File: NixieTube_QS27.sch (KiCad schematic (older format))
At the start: 56 parts, among them J1 Conn_01x06_Male, J2 HV_IN, J3 Conn_01x06_Female, J4 HV_OUT, Q1 MMBTA42LT1, Q10 MMBTA42LT1, Q11 AO3400, Q12 AO3400, Q13 AO3400, Q14 MMBTA42LT1, Q15 MMBTA42LT1, Q2 MMBTA42LT1, Q3 MMBTA42LT1, Q4 MMBTA42LT1, Q5 MMBTA42LT1, Q6 MMBTA42LT1, Q7 MMBTA42LT1, Q8 MMBTA42LT1, Q9 MMBTA42LT1, U1 74HC595D, U2 nixie-tube-qs27, U3 74HC595D, U4 ams1117-5.0

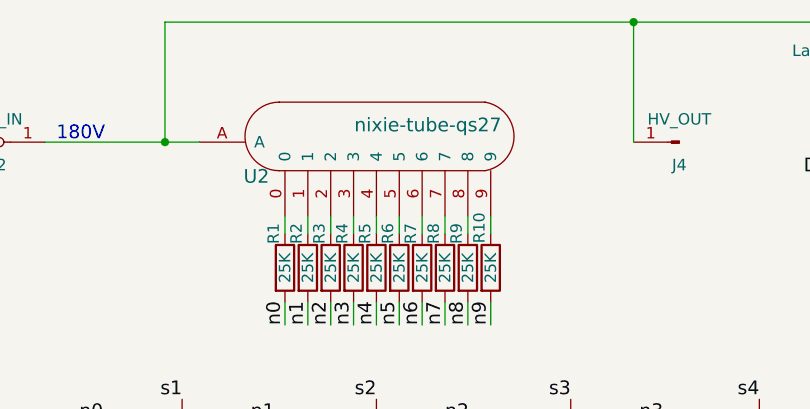
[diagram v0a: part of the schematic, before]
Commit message: checked all components, adjusted tracks
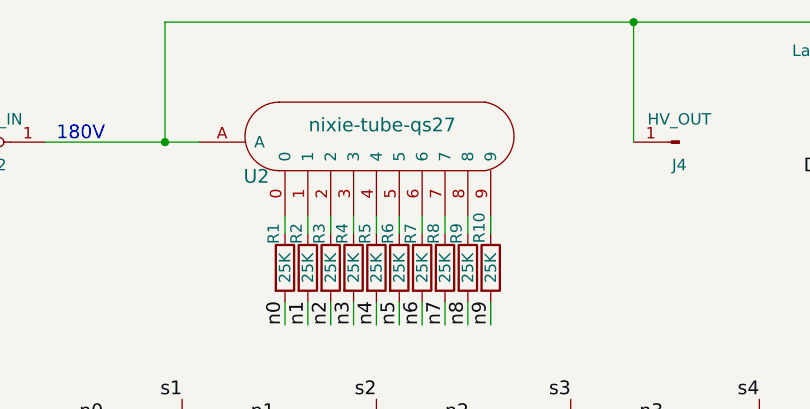
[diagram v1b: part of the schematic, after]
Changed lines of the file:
@@
 LIBS:valves
 LIBS:nixie-tube
-LIBS:Nixie-Tube-with-shiftR-cache
 EELAYER 25 0
 EELAYER END
@@
 P 5450 1950
 F 0 "U2" H 4875 2050 60  0000 C CNN
-F 1 "nixie-tube-qs27" H 5625 2275 60  0000 C CNN
+F 1 "nixie-tube-qs27" H 5425 2275 60  0000 C CNN
 F 2 "nixie-tube-fp:qs27-1" H 5150 1975 60  0001 C CNN
 F 3 "" H 5150 1975 60  0001 C CNN
